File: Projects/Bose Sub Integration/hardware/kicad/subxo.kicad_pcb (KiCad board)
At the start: 2 copper layers, 120 x 100 mm, 38 parts, among them J1 IN L, J2 IN R, J3 OUT 3.5mm, J4 PWR IN 15V, J5 POLARITY SW, J6 LEVEL POT 10k, U1 TL074, U2 LM7812

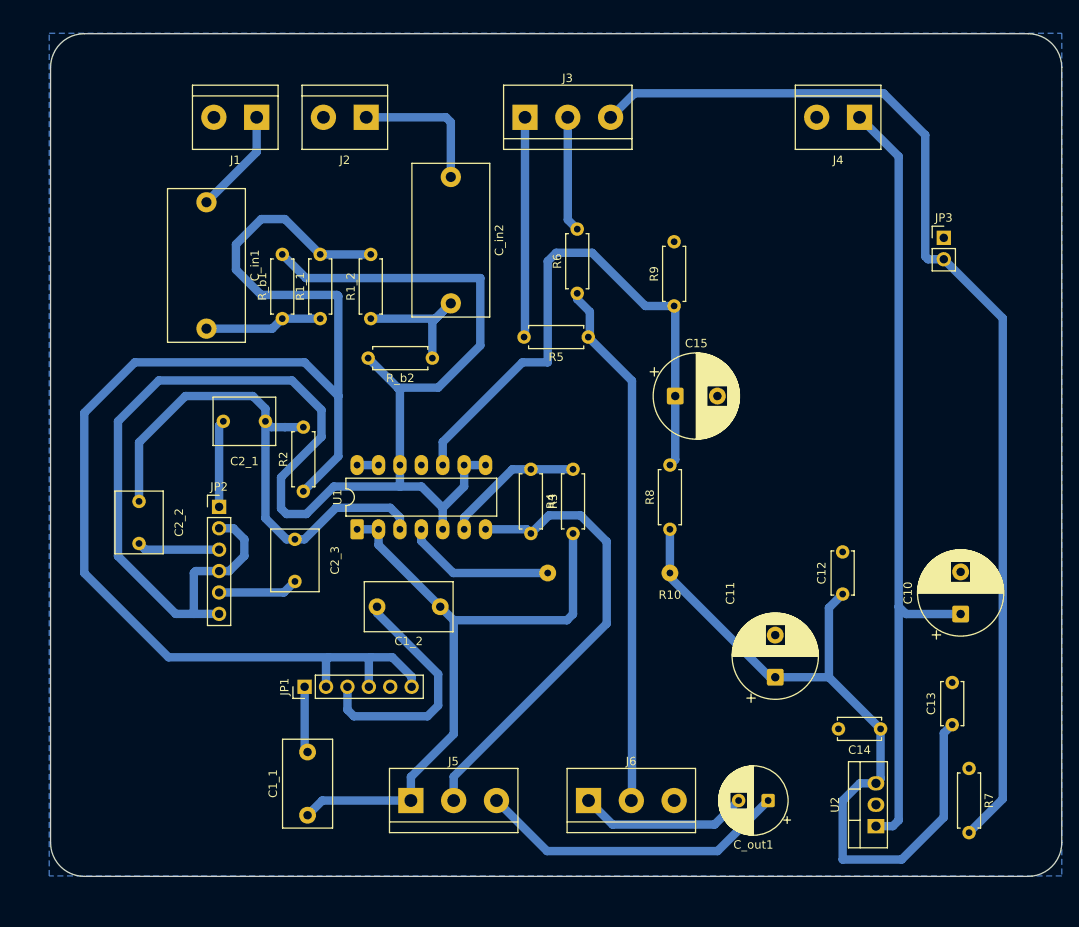
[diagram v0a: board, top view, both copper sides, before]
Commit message: Sub crossover board: re-placed, and the wire link is gone
The board committed in 28a28b6 only closed single-sided with R10, a 0 ohm
link flying over the tracks that sealed off U1 pin 4. Re-placing the parts
dissolves that pocket: /V12 now reaches pin 4 in copper. R10, the /V12_LNK
net it needed and the PWR_FLAG that marked that net as driven are all gone
from both the schematic and the layout.

185 track segments, every one on B.Cu, no vias and no top copper. DRC
reports 0 unconnected pads. The 15 violations that remain are silkscreen
only -- 12 overlaps and 3 clipped by mask -- and silkscreen is not in the
etched artwork, so none of them reach the board.

Outline comes down from 120.05 x 100.05 mm to 96.90 x 100.20 mm.

Zone rules now match the process instead of the KiCad defaults: minimum
clearance 0.5 -> 0.85 mm, and pads connect solid rather than through
thermal spokes.

Production files re-exported for the single-sided flow: B.Cu and Edge_Cuts
only, plus PTH drills, 100 holes across 0.8 / 1.0 / 1.1 / 1.2 / 1.52 mm.
The old two-sided set is dropped -- F.Cu, both solder masks, silkscreen and
the fab layer were never going to be made. The NPTH file exports empty.
Schematic is migrated to the KiCad 10 file format and stamped rev A.
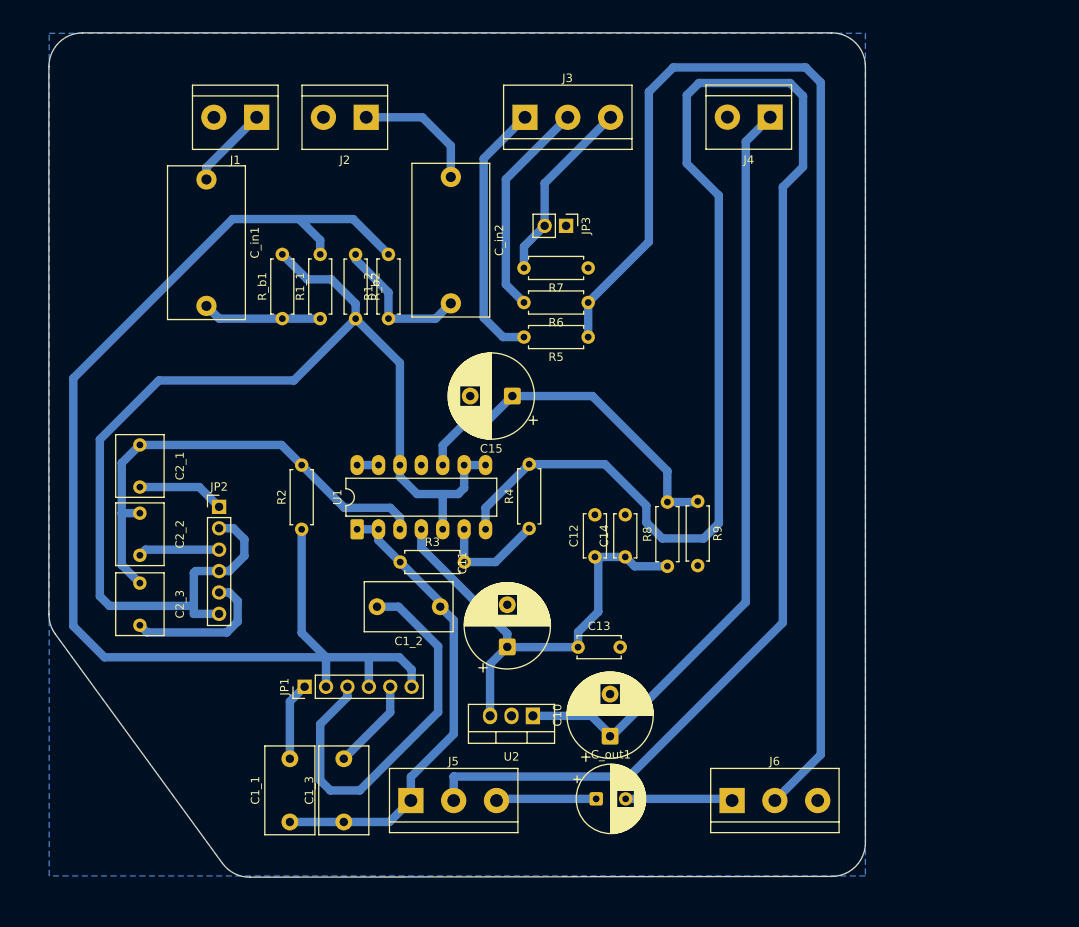
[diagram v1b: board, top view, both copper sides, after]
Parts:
- removed R10: 0R wire link, energy_system:WireLink_P14.50mm
- added C1_3: 150nF film, Capacitor_THT:C_Rect_L10.3mm_W5.7mm_P7.50mm_MKS4, F.Cu at (119.8, 130.5)
- moved R7 74.6 mm to (148.8, 64.8), turned to 180 degrees
- moved C13 45.3 mm to (147.6, 109.8), turned to 0 degrees
- moved JP3 44.8 mm to (146.2, 59.8), turned to -90 degrees
- moved C10 44.1 mm to (151.4, 120.4)
- moved U2 42.8 mm to (142.2, 118.0), turned to 180 degrees
- moved C14 36.5 mm to (153.2, 99.1), turned to 90 degrees
- moved C11 32.0 mm to (139.2, 109.8)
- moved C12 29.7 mm to (149.6, 99.1)
- moved R9 23.4 mm to (161.8, 92.5), turned to -90 degrees
- moved R3 20.8 mm to (126.5, 99.7), turned to 0 degrees
- moved C_out1 20.4 mm to (149.7, 127.8), turned to 0 degrees
- moved C15 19.3 mm to (139.8, 80.0), turned to 180 degrees
- moved C2_3 19.1 mm to (95.6, 102.2)
- moved J6 17.0 mm to (165.9, 128.0)
- moved R_b2 15.3 mm to (121.2, 63.2), turned to -90 degrees
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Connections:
- U1 pad 4: /V12_LNK -> /V12
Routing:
- net /OUT2: track 55.0 -> 218.3 mm
- net /OUT_GND: track 129.9 -> 22.1 mm
- net /POT_W: track 63.1 -> 141.9 mm
- net /VGND: track 183.8 -> 138.8 mm
- net /V12: track 92.7 -> 56.6 mm
- net /VG_DIV: track 68.3 -> 42.4 mm
- net /SW_COM: track 37.2 -> 11.9 mm
- net /OUT1: track 77.5 -> 56.0 mm
- net /C1B_SEL: track 29.1 -> 47.8 mm
- net /V12_LNK: track 18.0 -> 0.00 mm
- net /N1: track 166.0 -> 149.4 mm
- net /OUT_RING: track 13.7 -> 25.9 mm
- net /C1C_SEL: track 0.00 -> 10.8 mm
- net /C2C_SEL: track 9.54 -> 17.6 mm
- net /POT_TOP: track 20.2 -> 12.7 mm
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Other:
- board size 120 x 100 mm -> 96.9 x 100.2 mm

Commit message: Sub crossover: bridge the split ground pour with a wire link
The GND pour fills as two islands. The power corner -- J4, U2, C10 to C14, R9 --
is walled off from the rest of the board by the ring of parts around it. The two
come within 2.70 mm of each other beside U2.3, close enough to be worth trying
to close, so I moved U2 by plus and minus 3 mm in both axes and re-filled: still
two islands every time. The wall is the whole component ring, not that one pad.

So LK1 bridges them on an insulated wire, and GND splits into GND and GND_LNK to
match. The split is what makes a wire link work at all -- with one net on both
pads KiCad cannot know the wire is there and keeps reporting the island. Net
membership is taken from KiCad's own zone fill rather than guessed, and it is
placement-dependent: move parts and it has to be re-derived.

Each segment now carries its own PWR_FLAG, or ERC calls it undriven. And two
ground nets means two zones, since island_removal_mode 0 would otherwise delete
the power corner as an island with no pad of the zone's net.

Also withdrew the dual-pitch C_in footprint added earlier today. Its two
same-numbered pads sat 5 mm apart with no copper joining them; stock multi-pitch
footprints only work because their alternate pads overlap into one blob, and
duplicate_pad_numbers_are_jumpers defaults to no with no stock footprint in
KiCad 10 setting it. It bought nothing either, because a 2u2 film is 15 mm pitch
like the 220n, so the plain stock footprint rev A already had covers both.

ERC 0 errors, verify_netlist 118 of 118.
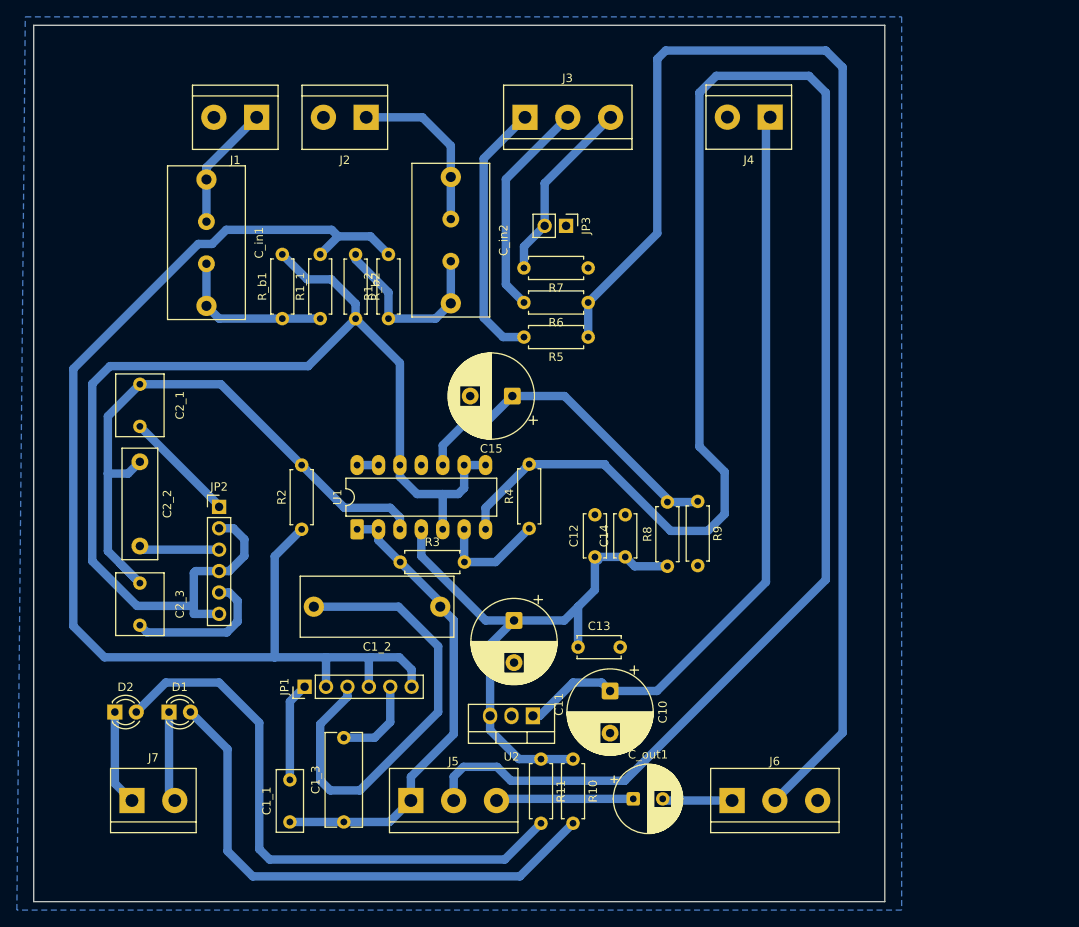
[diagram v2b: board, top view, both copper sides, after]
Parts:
- added D1: PWR green, LED_THT:LED_D3.0mm, F.Cu at (99.1, 117.5)
- added D2: INV amber, LED_THT:LED_D3.0mm, F.Cu at (92.6, 117.5)
- added J7: INV LED, TerminalBlock:TerminalBlock_bornier-2_P5.08mm, F.Cu at (94.7, 128.0)
- added R10: 4k7, Resistor_THT:R_Axial_DIN0207_L6.3mm_D2.5mm_P7.62mm_Horizontal, F.Cu at (147.0, 123.1)
- added R11: 4k7, Resistor_THT:R_Axial_DIN0207_L6.3mm_D2.5mm_P7.62mm_Horizontal, F.Cu at (143.2, 123.1)
- C1_1: value 330nF film -> 470nF film; footprint Capacitor_THT:C_Rect_L10.3mm_W5.7mm_P7.50mm_MKS4 -> Capacitor_THT:C_Rect_L7.2mm_W3.0mm_P5.00mm_FKS2_FKP2_MKS2_MKP2
- C1_2: footprint Capacitor_THT:C_Rect_L10.3mm_W5.7mm_P7.50mm_MKS4 -> Capacitor_THT:C_Rect_L18.0mm_W7.0mm_P15.00mm_FKS3_FKP3
- C1_3: footprint Capacitor_THT:C_Rect_L10.3mm_W5.7mm_P7.50mm_MKS4 -> Capacitor_THT:C_Rect_L11.0mm_W4.2mm_P10.00mm_MKT
- C2_2: value 100nF film -> 120nF film; footprint Capacitor_THT:C_Rect_L7.2mm_W5.5mm_P5.00mm_FKS2_FKP2_MKS2_MKP2 -> Capacitor_THT:C_Rect_L13.0mm_W4.0mm_P10.00mm_FKS3_FKP3_MKS4
- C_in1, C_in2: value 2.2uF film -> 220n or 2u2; footprint Capacitor_THT:C_Rect_L18.0mm_W9.0mm_P15.00mm_FKS3_FKP3 -> energy_system:C_Rect_L18.0mm_W9.0mm_P5.00mm_P15.00mm_MultiPitch
- moved C2_1 7.20 mm to (95.6, 78.6)
- moved C2_2 6.10 mm to (95.6, 87.8)
- moved C10 5.37 mm to (151.4, 115.0), turned to -90 degrees
- moved C_out1 4.40 mm to (154.1, 127.8)
- moved C11 3.24 mm to (140.0, 106.6), turned to -90 degrees
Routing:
- net /INV_A: track 0.00 -> 68.7 mm
- net /PWR_A: track 0.00 -> 63.2 mm
- net /N2: track 56.2 -> 73.3 mm
- net /V12: track 56.6 -> 72.2 mm
- net /INV_K: track 0.00 -> 11.3 mm
- net /GND: track 0.00 -> 10.8 mm
- net /POT_W: track 141.9 -> 150.0 mm
- net /C1B_SEL: track 47.8 -> 55.3 mm
- net /IN_R: track 15.1 -> 20.1 mm
- net /IN_L: track 9.85 -> 14.8 mm
- net /A_R: track 17.4 -> 22.4 mm
- net /A_L: track 14.1 -> 19.1 mm
- net /SW_COM: track 11.9 -> 16.3 mm
- net /POT_TOP: track 12.7 -> 8.59 mm
- net /VGND: track 138.8 -> 142.0 mm
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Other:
- board size 96.9 x 100.2 mm -> 101 x 104 mm

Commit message: Sub crossover: widen the LED footprint so it clears the milling rule
The only real DRC errors on the hand-placed board were the two status LEDs:
2.54 mm pitch against 1.8 mm pads leaves 0.74 mm between them, under the
0.85 mm rule and nowhere near the 1.2 mm a 0.8 mm endmill would want. Four
violations, two per LED, reported once from each side.

There is no stock footprint to switch to. Every two-pad part in LED_THT uses the
same 2.54/1.8 geometry, so this is a project footprint.

LED legs bend freely, so the pitch is the lever to pull rather than the pad
size -- the opposite of the TO-220, whose pitch is fixed and whose pads had to
be narrowed to 1.7 mm instead. 5.08 mm pitch with 2.0 mm pads gives a 3.08 mm
channel, which clears either process with room to spare and leaves a generous
annular ring for milling. 2.54 mm of total splay is nothing for an LED.

Drill stays 0.8 mm, already the commonest size on the board.
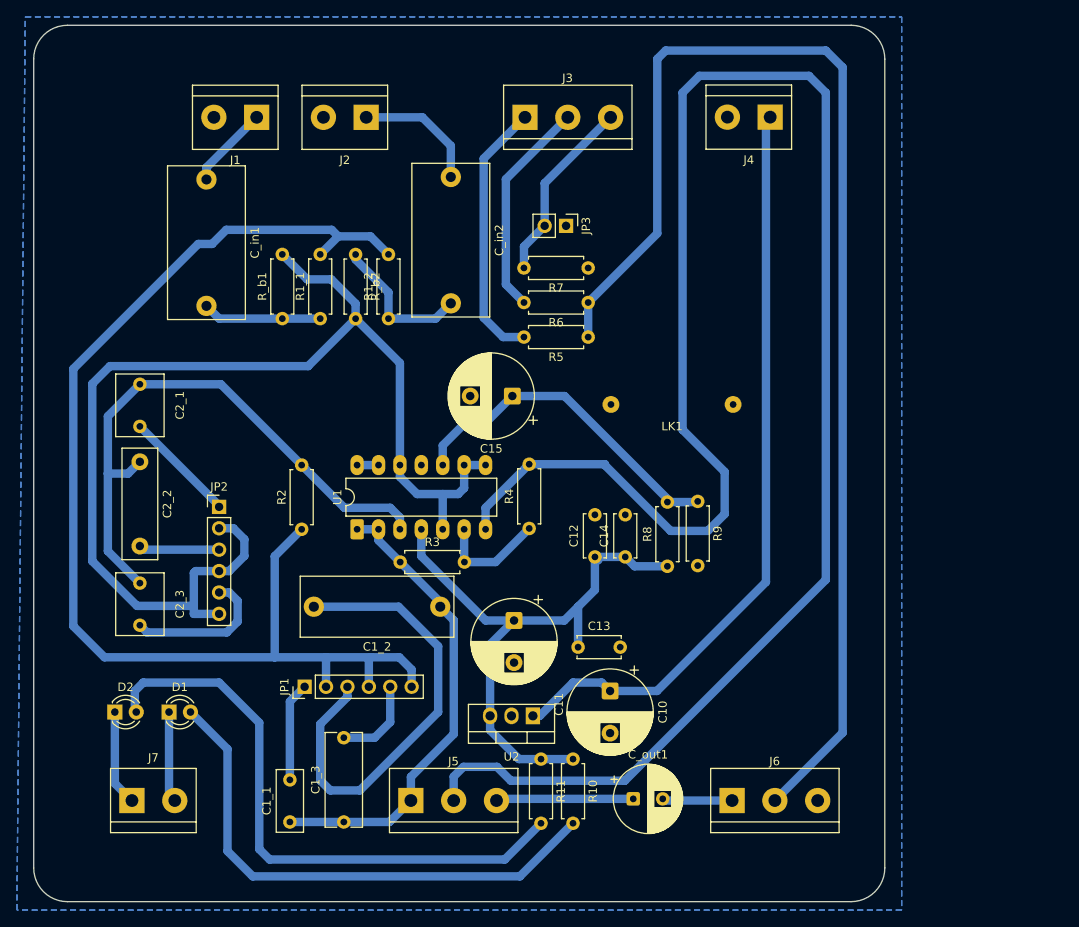
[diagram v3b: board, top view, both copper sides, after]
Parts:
- added LK1: 0R wire link, energy_system:WireLink_P14.50mm, F.Cu at (166.0, 81.0)
- C_in1, C_in2: footprint energy_system:C_Rect_L18.0mm_W9.0mm_P5.00mm_P15.00mm_MultiPitch -> Capacitor_THT:C_Rect_L18.0mm_W9.0mm_P15.00mm_FKS3_FKP3
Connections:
- C10 pad 2: /GND -> /GND_LNK
- C11 pad 2: /GND -> /GND_LNK
- C12 pad 2: /GND -> /GND_LNK
- C13 pad 2: /GND -> /GND_LNK
- C14 pad 2: /GND -> /GND_LNK
- J4 pad 2: /GND -> /GND_LNK
- R9 pad 2: /GND -> /GND_LNK
- U2 pad 2: /GND -> /GND_LNK
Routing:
- net /IN_R: track 20.1 -> 15.1 mm
- net /IN_L: track 14.8 -> 9.85 mm
- net /A_R: track 22.4 -> 17.4 mm
- net /A_L: track 19.1 -> 14.1 mm
- net /N2: track 73.3 -> 69.9 mm
- net /OUT2: track 221.0 -> 223.8 mm
- net /INV_A: track 68.7 -> 70.5 mm
- added copper zone on B.Cu, net /GND_LNK
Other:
- outline, holes or cut-outs redrawn

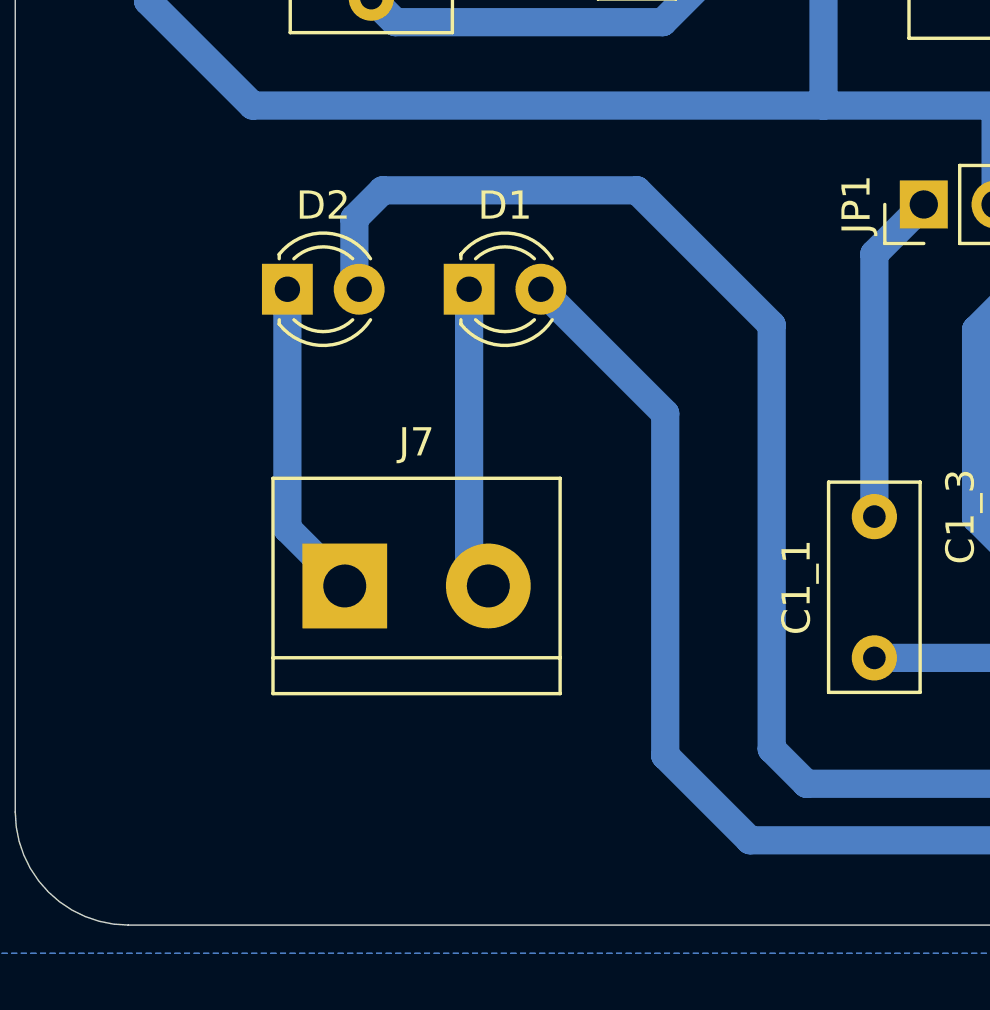
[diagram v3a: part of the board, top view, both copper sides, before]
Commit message: Sub crossover: hand placement of the rev B board
All 43 footprints placed by hand in the GUI, rev B netlist imported. Ground
pour bridged by LK1, so DRC reports zero unconnected items. The only remaining
violations are silkscreen: 17 overlaps and 4 silk-over-copper.

Snapshotting the placement before touching the silk, so the text moves can be
reverted without losing the layout.
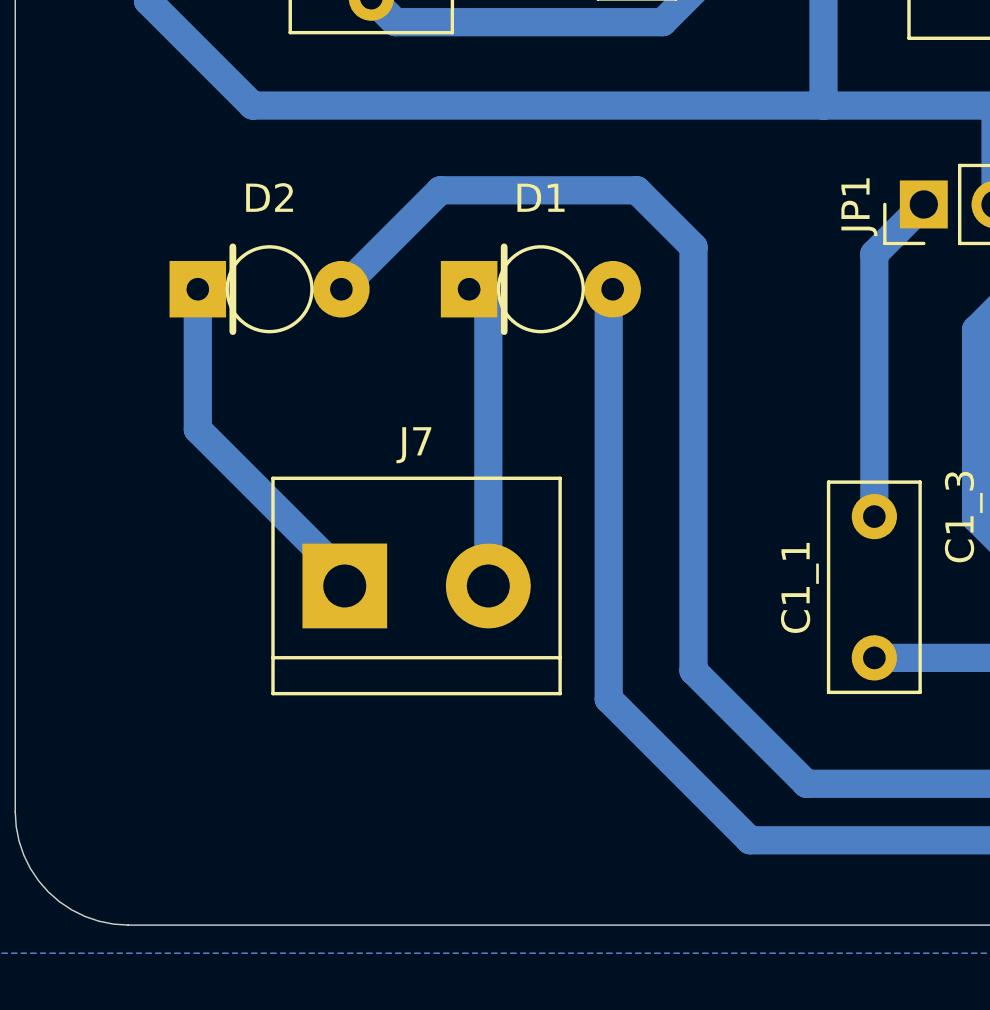
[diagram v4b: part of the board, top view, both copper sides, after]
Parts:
- D1, D2: footprint LED_THT:LED_D3.0mm -> energy_system:LED_D3.0mm_P5.08mm_LaserPads
- moved D2 3.17 mm to (89.5, 117.5)
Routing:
- net /INV_K: track 11.3 -> 12.7 mm
- net /INV_A: track 70.5 -> 69.4 mm
- net /GND: track 10.8 -> 11.7 mm
- net /PWR_A: track 63.2 -> 62.2 mm
